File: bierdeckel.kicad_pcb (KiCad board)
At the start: 2 copper layers, 93 x 93 mm, 60 parts, among them J1 S70-332002045R, J2 S70-332002045R, J3 S70-332002045R, J4 S70-332002045R, SW1 Address Coding, SW2 PTS526 SK15 SMTR2 LFS, SW3 PTS526 SK15 SMTR2 LFS, U1 ESP32-C3-WROOM-02, U2 BQ25176J, U3 TPS61201DRC, U4 TLV9101IDBVR

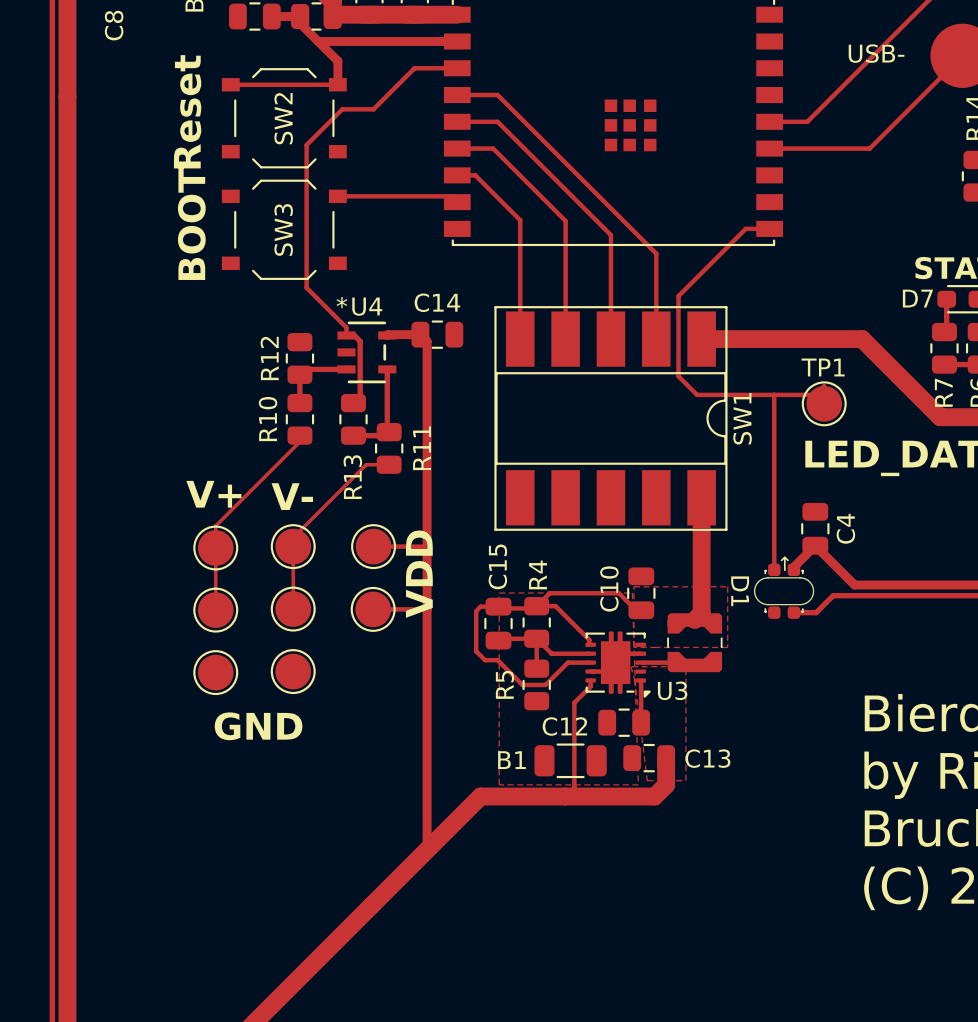
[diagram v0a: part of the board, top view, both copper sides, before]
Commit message: change to 2 pressure gauge strips
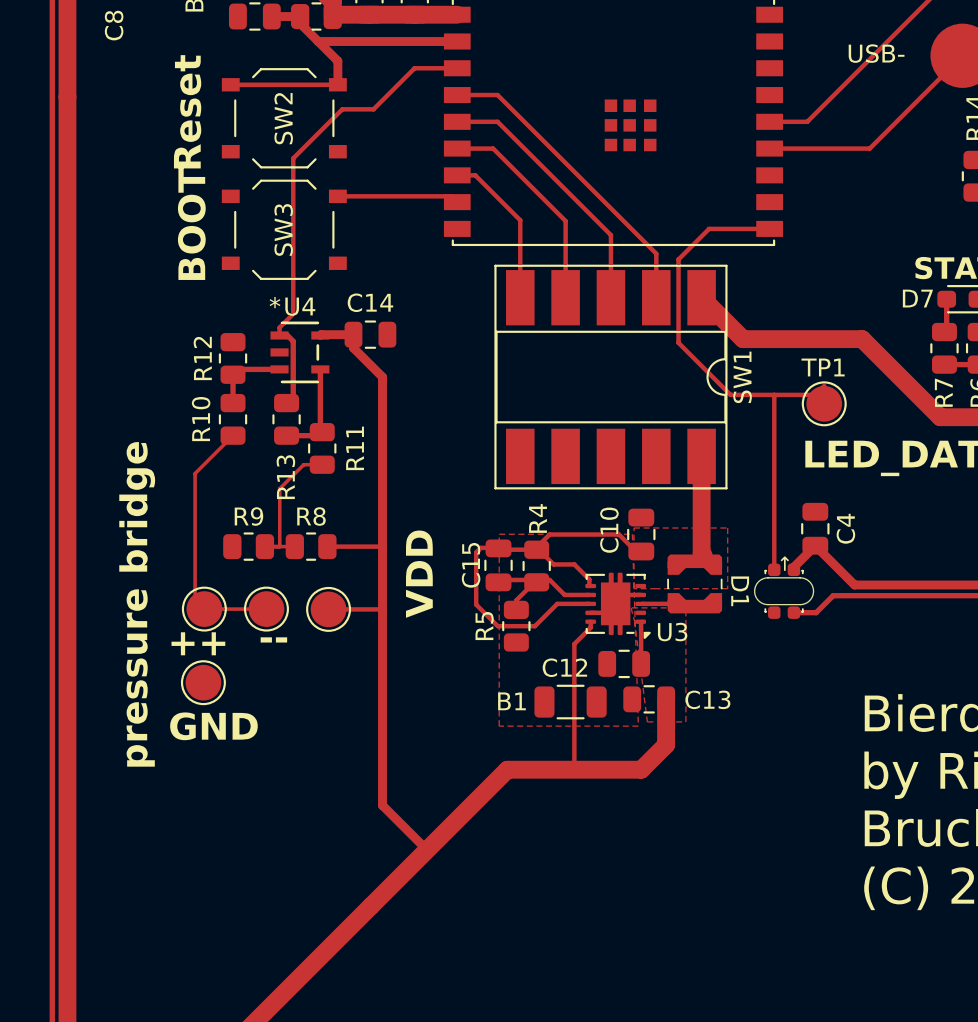
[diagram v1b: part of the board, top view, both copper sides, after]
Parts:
- removed TP6, TP7, TP8, TP9: TestPoint, TestPoint:TestPoint_Pad_D2.0mm
- added R8: 1k, Resistor_SMD:R_0805_2012Metric, F.Cu at (120.0, 94.0)
- added R9: 1k, Resistor_SMD:R_0805_2012Metric, F.Cu at (116.5, 94.0)
- moved C14 3.75 mm to (123.3, 82.1)
- moved R10 3.75 mm to (115.6, 86.9)
- moved R11 3.75 mm to (120.6, 88.5)
- moved R12 3.75 mm to (115.6, 83.5)
- moved R13 3.75 mm to (118.6, 86.9)
- moved U4 3.75 mm to (119.4, 83.1)
- moved R5 3.48 mm to (131.5, 98.5)
- moved TP11 3.48 mm to (114.0, 97.5), turned to 90 degrees
- moved B1 3.29 mm to (134.5, 102.7)
- moved C10 3.29 mm to (138.5, 93.3)
- moved C12 3.29 mm to (137.5, 100.6)
- moved L1 3.29 mm to (141.5, 96.1)
- moved U3 3.29 mm to (137.1, 97.2)
- moved C13 3.29 mm to (138.9, 102.6)
- moved C15 3.27 mm to (130.5, 95.0)
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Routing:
- net +3.3V: track 422.7 -> 427.9 mm
- net /Pressure Gauge/VR+: track 11.7 -> 14.3 mm
- net /Pressure Gauge/VR-: track 11.1 -> 8.69 mm
- net /AD3: track 17.1 -> 14.7 mm
- net /AD2: track 19.6 -> 17.3 mm
- net /AD1: track 11.2 -> 8.91 mm
- net /AD0: track 14.4 -> 12.0 mm
- net /Vbat: track 51.0 -> 52.0 mm
- net /Vreg_in: track 31.1 -> 30.1 mm
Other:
- board text added: "++"
- board text added: "--"
- board text added: "pressure bridge"
- board text removed: "V+"
- board text removed: "V-"

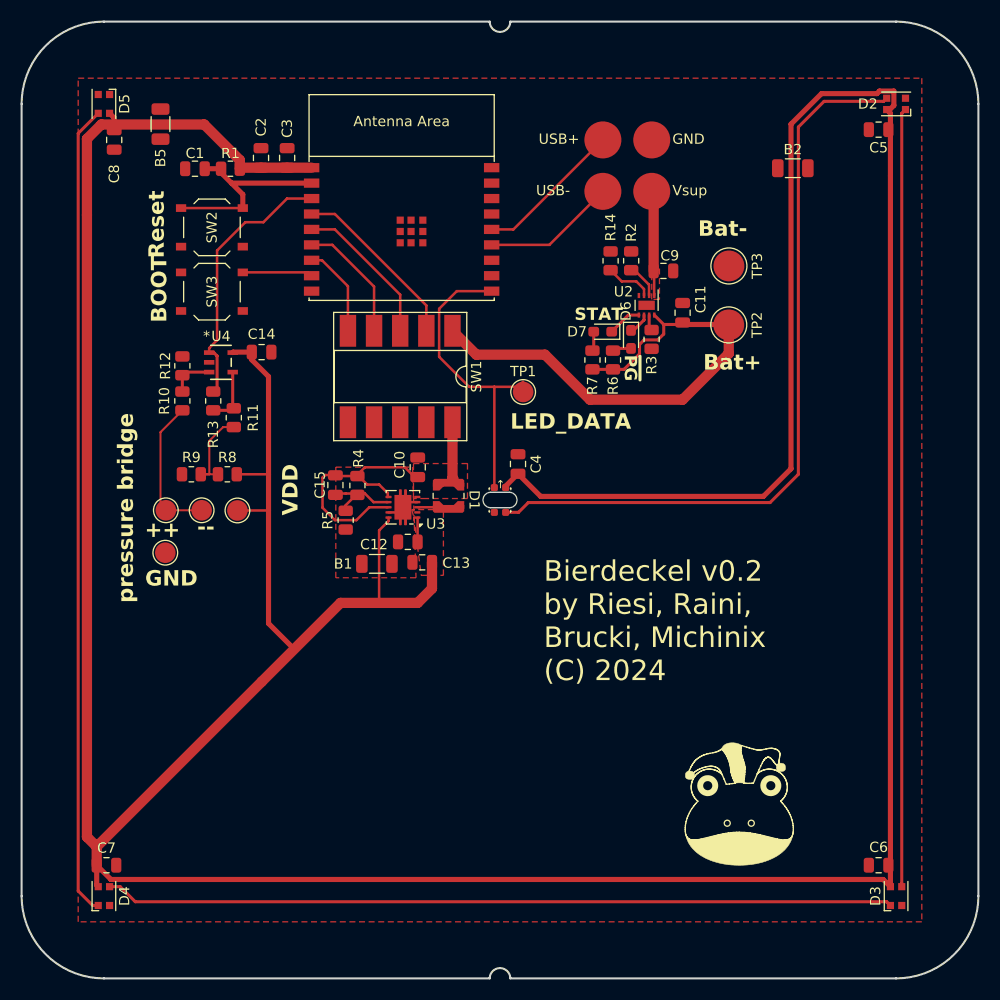
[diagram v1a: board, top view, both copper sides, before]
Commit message: update design; add 3d models to everything; add notches to PCB
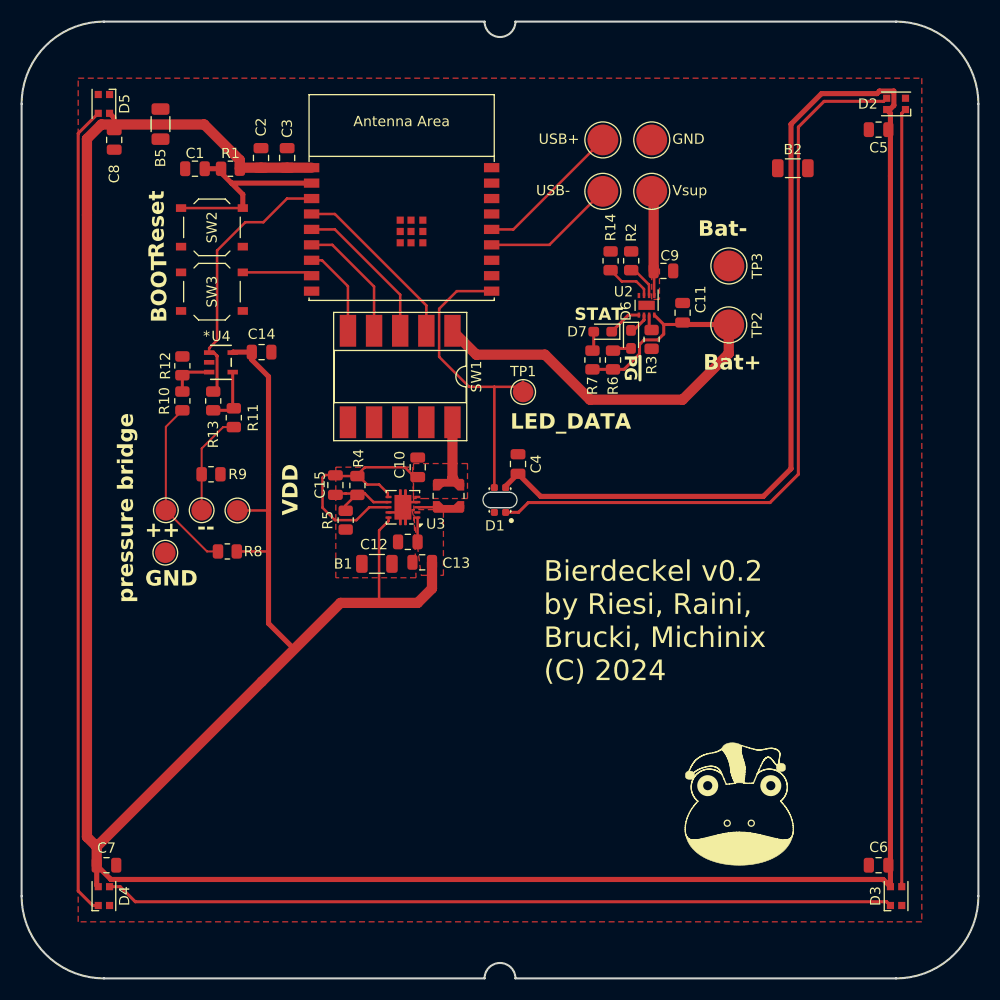
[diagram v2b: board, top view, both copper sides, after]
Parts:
- J1, J2, J3, J4: value S70-332002045R -> Pogo; footprint bier:pogo_receptor -> TestPoint:TestPoint_Pad_D3.0mm
- R8, R9: value 1k -> 350
- moved R8 7.50 mm to (120.0, 101.5)
- moved TP11 3.48 mm to (117.5, 97.5)
- moved TP4 3.48 mm to (114.0, 97.5)
- moved R9 1.91 mm to (118.4, 94.0), turned to 180 degrees
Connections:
- R8 pad 1: /Pressure Gauge/VR- -> /Pressure Gauge/VR+
- TP11 pad 1: /Pressure Gauge/VR+ -> /Pressure Gauge/VR-
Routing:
- net /Pressure Gauge/VR+: track 14.3 -> 17.8 mm
- net /Pressure Gauge/VR-: track 8.69 -> 9.99 mm
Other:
- outline, holes or cut-outs redrawn

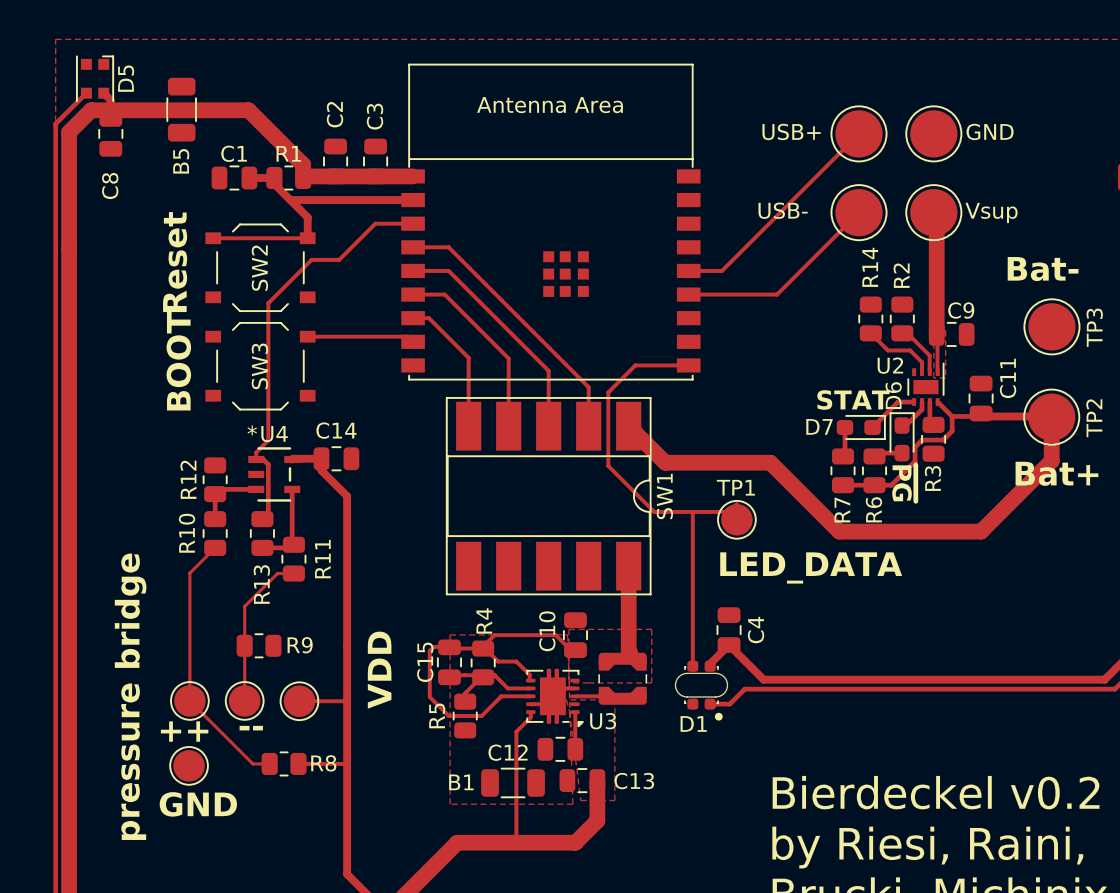
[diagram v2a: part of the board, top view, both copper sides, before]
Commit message: reannotate components and move some designators
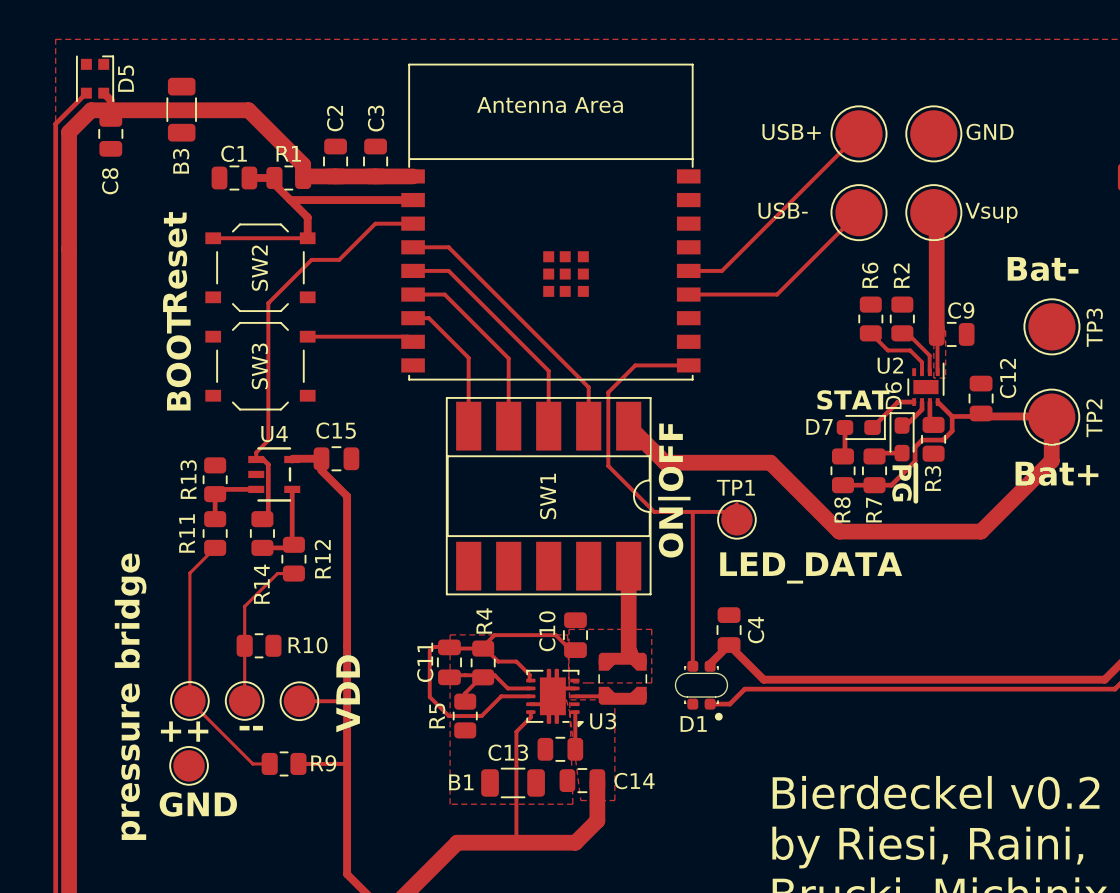
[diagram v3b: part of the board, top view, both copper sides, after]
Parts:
- renumbered B5 to B3, C15 to C11, C11 to C12, C12 to C13, C13 to C14, C14 to C15, R9 to R10, R10 to R11, R11 to R12, R12 to R13, R13 to R14, R14 to R6, R6 to R7, R7 to R8, R8 to R9, TP10 to TP6, TP11 to TP7
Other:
- board text added: "ON|OFF"
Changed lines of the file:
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@@
 		(descr "Capacitor SMD 0805 (2012 Metric), square (rectangular) end terminal, IPC_7351 nominal, (Body size source: IPC-SM-782 page 76, https://www.pcb-3d.com/wordpress/wp-content/uploads/ipc-sm-782a_amendment_1_and_2.pdf, https://docs.google.com/spreadsheets/d/1BsfQQcO9C6DZCsRaXUlFlo91Tg2WpOkGARC1WS5S8t0/edit?usp=sharing), generated with kicad-footprint-generator")
 		(tags "capacitor")
-		(property "Reference" "C11"
+		(property "Reference" "C12"
 			(at 1.3 1.75 -90)
 			(layer "F.SilkS")
@@
 		(tags "THT DIP DIL PDIP 2.54mm 8.89mm 350mil SMDSocket LongPads")
 		(property "Reference" "SW1"
-			(at 0 -7.41 90)
+			(at 0 0 90)
 			(layer "F.SilkS")
 			(effects
@@
 		(descr "Resistor SMD 0805 (2012 Metric), square (rectangular) end terminal, IPC_7351 nominal, (Body size source: IPC-SM-782 page 72, https://www.pcb-3d.com/wordpress/wp-content/uploads/ipc-sm-782a_amendment_1_and_2.pdf), generated with kicad-footprint-generator")
 		(tags "resistor")
-		(property "Reference" "R8"
+		(property "Reference" "R9"
 			(at 2.5 0 0)
 			(layer "F.SilkS")
@@
 		(descr "Resistor SMD 0805 (2012 Metric), square (rectangular) end terminal, IPC_7351 nominal, (Body size source: IPC-SM-782 page 72, https://www.pcb-3d.com/wordpress/wp-content/uploads/ipc-sm-782a_amendment_1_and_2.pdf), generated with kicad-footprint-generator")
 		(tags "resistor")
-		(property "Reference" "R9"
-			(at -2.5875 0 0)
+		(property "Reference" "R10"
+			(at -3.0875 0 0)
 			(layer "F.SilkS")
 			(effects
@@
 		(descr "Capacitor SMD 0805 (2012 Metric), square (rectangular) end terminal, IPC_7351 nominal, (Body size source: IPC-SM-782 page 76, https://www.pcb-3d.com/wordpress/wp-content/uploads/ipc-sm-782a_amendment_1_and_2.pdf, https://docs.google.com/spreadsheets/d/1BsfQQcO9C6DZCsRaXUlFlo91Tg2WpOkGARC1WS5S8t0/edit?usp=sharing), generated with kicad-footprint-generator")
 		(tags "capacitor")
-		(property "Reference" "C14"
+		(property "Reference" "C15"
 			(at 0 -1.75 0)
 			(layer "F.SilkS")
@@
 		(descr "Capacitor SMD 0805 (2012 Metric), square (rectangular) end terminal, IPC_7351 nominal, (Body size source: IPC-SM-782 page 76, https://www.pcb-3d.com/wordpress/wp-content/uploads/ipc-sm-782a_amendment_1_and_2.pdf, https://docs.google.com/spreadsheets/d/1BsfQQcO9C6DZCsRaXUlFlo91Tg2WpOkGARC1WS5S8t0/edit?usp=sharing), generated with kicad-footprint-generator")
 		(tags "capacitor")
-		(property "Reference" "C13"
+		(property "Reference" "C14"
 			(at -3.31 -0.065001 0)
 			(layer "F.SilkS")
@@
 		(descr "Resistor SMD 0805 (2012 Metric), square (rectangular) end terminal, IPC_7351 nominal, (Body size source: IPC-SM-782 page 72, https://www.pcb-3d.com/wordpress/wp-content/uploads/ipc-sm-782a_amendment_1_and_2.pdf), generated with kicad-footprint-generator")
 		(tags "resistor")
-		(property "Reference" "R11"
+		(property "Reference" "R12"
 			(at 0 1.874998 -90)
 			(layer "F.SilkS")
@@
 		(descr "SMD pad as test Point, diameter 2.0mm")
 		(tags "test point SMD pad")
-		(property "Reference" "TP11"
+		(property "Reference" "TP7"
 			(at -3.180681 -0.073504 90)
 			(layer "F.SilkS")
@@
 		(descr "SMD pad as test Point, diameter 2.0mm")
 		(tags "test point SMD pad")
-		(property "Reference" "TP10"
+		(property "Reference" "TP6"
 			(at 2.021793 -0.018312 90)
 			(layer "F.SilkS")
@@
 		(descr "Resistor SMD 0805 (2012 Metric), square (rectangular) end terminal, IPC_7351 nominal, (Body size source: IPC-SM-782 page 72, https://www.pcb-3d.com/wordpress/wp-content/uploads/ipc-sm-782a_amendment_1_and_2.pdf), generated with kicad-footprint-generator")
 		(tags "resistor")
-		(property "Reference" "R12"
+		(property "Reference" "R13"
 			(at 0 -1.65 -90)
 			(layer "F.SilkS")
@@
 		(descr "Resistor SMD 0805 (2012 Metric), square (rectangular) end terminal, IPC_7351 nominal, (Body size source: IPC-SM-782 page 72, https://www.pcb-3d.com/wordpress/wp-content/uploads/ipc-sm-782a_amendment_1_and_2.pdf), generated with kicad-footprint-generator")
 		(tags "resistor")
-		(property "Reference" "R7"
+		(property "Reference" "R8"
 			(at -2.5 0 90)
 			(layer "F.SilkS")
@@
 		(tags "capacitor")
 		(property "Reference" "C2"
-			(at 3 0 90)
+			(at 2.75 0.009326 90)
 			(layer "F.SilkS")
 			(effects
@@
 		(descr "Resistor SMD 0805 (2012 Metric), square (rectangular) end terminal, IPC_7351 nominal, (Body size source: IPC-SM-782 page 72, https://www.pcb-3d.com/wordpress/wp-content/uploads/ipc-sm-782a_amendment_1_and_2.pdf), generated with kicad-footprint-generator")
 		(tags "resistor")
-		(property "Reference" "R13"
+		(property "Reference" "R14"
 			(at -3.25 0 -90)
 			(layer "F.SilkS")
@@
 		(descr "Resistor SMD 0805 (2012 Metric), square (rectangular) end terminal, IPC_7351 nominal, (Body size source: IPC-SM-782 page 72, https://www.pcb-3d.com/wordpress/wp-content/uploads/ipc-sm-782a_amendment_1_and_2.pdf), generated with kicad-footprint-generator")
 		(tags "resistor")
-		(property "Reference" "R6"
+		(property "Reference" "R7"
 			(at -2.5 0 90)
 			(layer "F.SilkS")
@@
 		(descr "Resistor SMD 0805 (2012 Metric), square (rectangular) end terminal, IPC_7351 nominal, (Body size source: IPC-SM-782 page 72, https://www.pcb-3d.com/wordpress/wp-content/uploads/ipc-sm-782a_amendment_1_and_2.pdf), generated with kicad-footprint-generator")
 		(tags "resistor")
-		(property "Reference" "R10"
+		(property "Reference" "R11"
 			(at -0.004307 -1.749999 -90)
 			(layer "F.SilkS")
@@
 		(descr "Capacitor SMD 0805 (2012 Metric), square (rectangular) end terminal, IPC_7351 nominal, (Body size source: IPC-SM-782 page 76, https://www.pcb-3d.com/wordpress/wp-content/uploads/ipc-sm-782a_amendment_1_and_2.pdf, https://docs.google.com/spreadsheets/d/1BsfQQcO9C6DZCsRaXUlFlo91Tg2WpOkGARC1WS5S8t0/edit?usp=sharing), generated with kicad-footprint-generator")
 		(tags "capacitor")
-		(property "Reference" "C12"
+		(property "Reference" "C13"
 			(at 3.29 -0.25 0)
 			(layer "F.SilkS")
@@
 		(descr "Resistor SMD 1206 (3216 Metric), square (rectangular) end terminal, IPC_7351 nominal, (Body size source: IPC-SM-782 page 72, https://www.pcb-3d.com/wordpress/wp-content/uploads/ipc-sm-782a_amendment_1_and_2.pdf), generated with kicad-footprint-generator")
 		(tags "resistor")
-		(property "Reference" "B5"
+		(property "Reference" "B3"
 			(at -3.2875 0 90)
 			(layer "F.SilkS")
@@
 			(unlocked yes)
 			(layer "F.SilkS")
-			(effects
-				(font
-					(size 1 1)
-					(thickness 0.15)
-				)
-			)
-		)
-		(fp_text user "*"
-			(at -1.397 -2.5502 0)
-			(unlocked yes)
-			(layer "F.SilkS")
 			(hide yes)
 			(effects
@@
 			(pintype "power_in")
 		)
+		(model "${KICAD8_3DMODEL_DIR}/Package_TO_SOT_SMD.3dshapes/SOT-23-5.wrl"
+			(offset
+				(xyz 0 0 0)
+			)
+			(scale
+				(xyz 1 1 1)
+			)
+			(rotate
+				(xyz 0 0 0)
+			)
+		)
 	)
 	(footprint "Resistor_SMD:R_0805_2012Metric"
@@
 		(tags "capacitor")
 		(property "Reference" "C3"
-			(at 2.86 0 90)
+			(at 2.739627 0.067515 90)
 			(layer "F.SilkS")
 			(effects
@@
 		(descr "Resistor SMD 0805 (2012 Metric), square (rectangular) end terminal, IPC_7351 nominal, (Body size source: IPC-SM-782 page 72, https://www.pcb-3d.com/wordpress/wp-content/uploads/ipc-sm-782a_amendment_1_and_2.pdf), generated with kicad-footprint-generator")
 		(tags "resistor")
-		(property "Reference" "R14"
-			(at -3.25 0 90)
+		(property "Reference" "R6"
+			(at -2.75 0 90)
 			(layer "F.SilkS")
 			(effects
@@
 		(descr "Capacitor SMD 0805 (2012 Metric), square (rectangular) end terminal, IPC_7351 nominal, (Body size source: IPC-SM-782 page 76, https://www.pcb-3d.com/wordpress/wp-content/uploads/ipc-sm-782a_amendment_1_and_2.pdf, https://docs.google.com/spreadsheets/d/1BsfQQcO9C6DZCsRaXUlFlo91Tg2WpOkGARC1WS5S8t0/edit?usp=sharing), generated with kicad-footprint-generator")
 		(tags "capacitor")
-		(property "Reference" "C15"
+		(property "Reference" "C11"
 			(at -0.022499 1.5 90)
 			(layer "F.SilkS")
@@
 		(tags "capacitor")
 		(property "Reference" "C8"
-			(at 3.3 0 90)
+			(at 3 0 90)
 			(layer "F.SilkS")
 			(effects
@@
 	)
 	(gr_text "VDD"
-		(at 127 98 90)
+		(at 125 99.5 90)
+		(layer "F.SilkS")
+		(effects
+			(font
+				(size 1.5 1.5)
+				(thickness 0.3)
+				(bold yes)
+			)
+			(justify left bottom)
+		)
+	)
+	(gr_text "ON|OFF"
+		(at 145.5 88.5 90)
 		(layer "F.SilkS")
 		(effects
